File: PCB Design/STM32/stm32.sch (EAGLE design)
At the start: 54 parts, among them Q1 8MHz, T1 SFH303, T2 SFH303, T3 SFH303, T4 SFH303, U1 STM32F103RET6, U2 MCP1700T-3302E/TT, U3 MCP1700T-3302E/TT, U4 MPU-6000QFN-24, U5 TB6612FNG

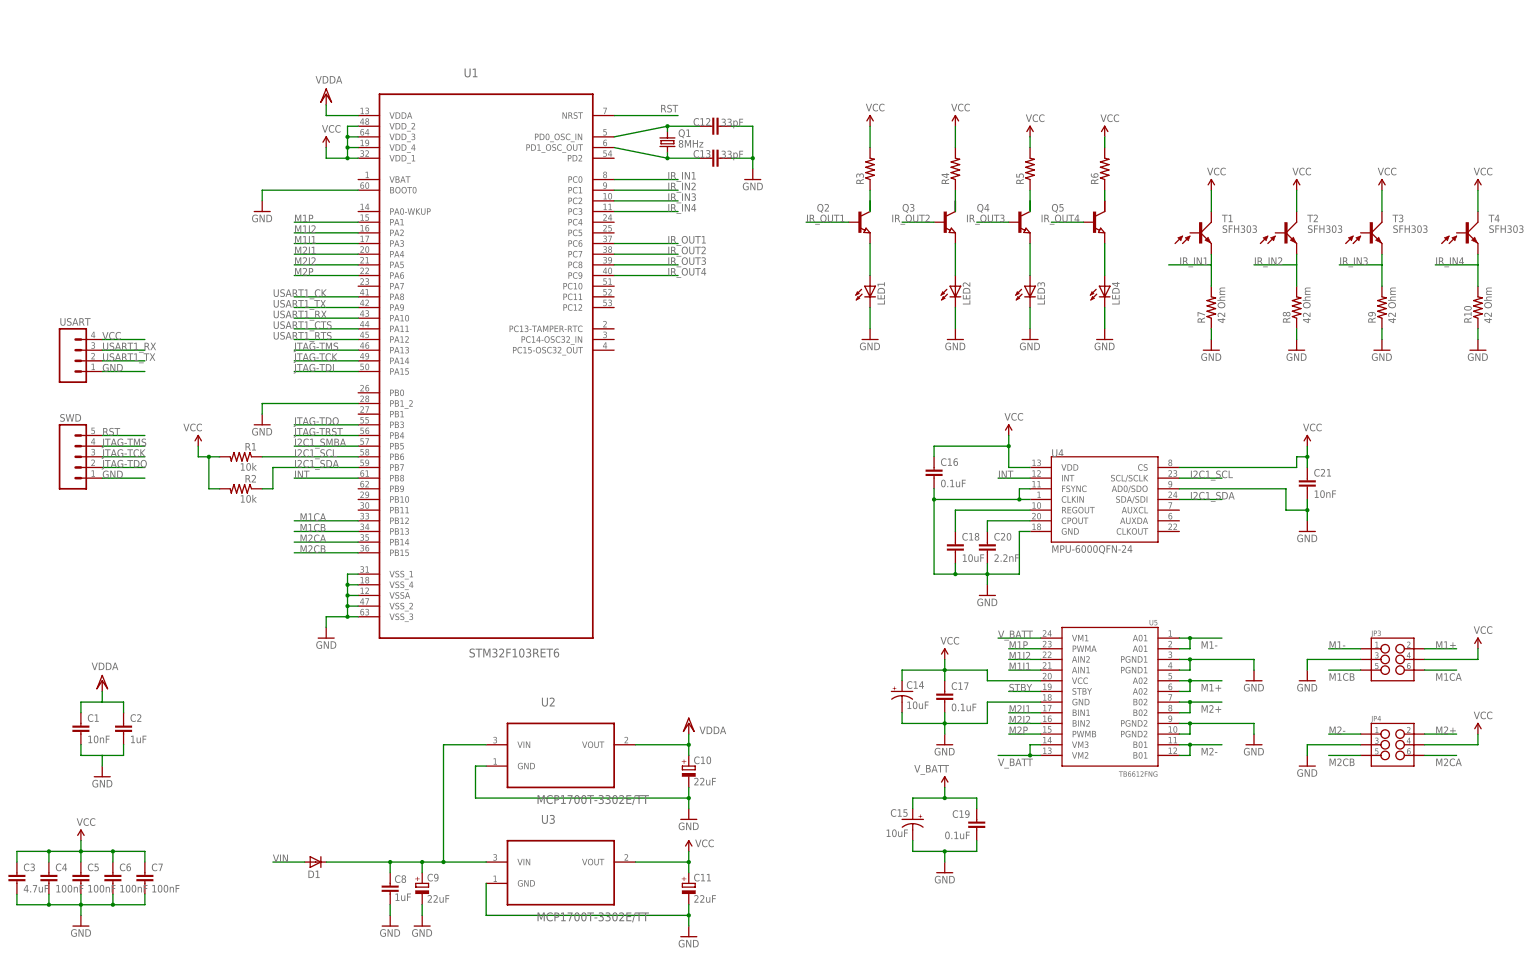
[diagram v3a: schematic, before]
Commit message: add 5v regulator
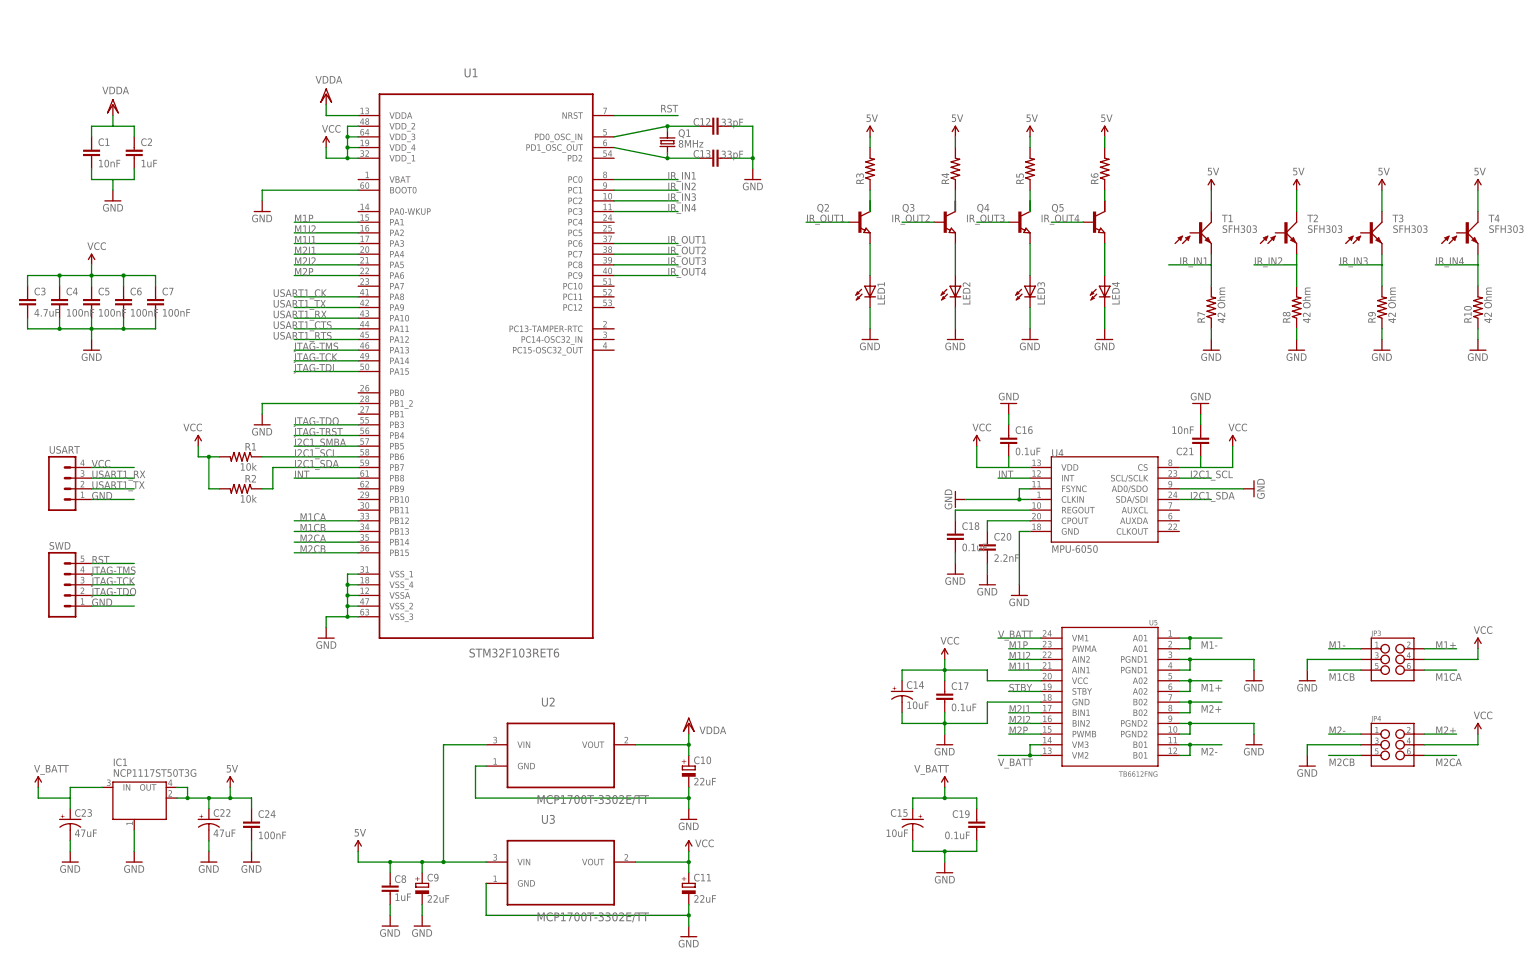
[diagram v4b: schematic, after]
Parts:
- removed D1: (no value), diode:DIODE-SOD323-W
- added C22, C23: 47uF, SparkFun-Capacitors:CAP_POLD
- added C24: 100nF, SparkFun-Capacitors:CAP0603-CAP
- added IC1: NCP1117ST50T3G, linear:MC33269ST-3.3T3
- C18: value 10uF -> 0.1uF
- U4: value MPU-6000QFN-24 -> MPU-6050
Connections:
- removed net N$1: C8.2, C9.+, D1.C, U2.VIN, U3.VIN
- removed net VIN: D1.A
- new net 5V: C22.+, C24.1, C8.2, C9.+, IC1.OUT, IC1.OUT@1, R3.2, R4.2, R5.2, R6.2, T1.C, T2.C, T3.C, T4.C, U2.VIN, U3.VIN
- net GND: now also C16.1, C22.-, C23.-, C24.2, IC1.GND/ADJ; no longer C16.2
- net VCC: now also C16.2; no longer C16.1, R3.2, R4.2, R5.2, R6.2, T1.C, T2.C, T3.C, T4.C
- net V_BATT: now also C23.+, IC1.IN
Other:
- moved on the sheet: C1, C16, C18, C2, C21, C3, C4, C5, C6, C7, SWD, USART

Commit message: refine connection
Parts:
- removed C14: 10uF, SparkFun-Capacitors:CAP_POL1206
- removed C24: 100nF, SparkFun-Capacitors:CAP0603-CAP
- removed C8: 1uF, SparkFun:CAP0603
- C12, C13: device SparkFun:CAP0603 -> SparkFun-Capacitors:CAP0603-CAP
- C15: device SparkFun-Capacitors:CAP_POL1206 -> SparkFun-Capacitors:CAP_POL1206-KIT
- C2: device SparkFun-Capacitors:CAP0603-CAP -> SparkFun-Capacitors:CAP0805
- C22, C23: value 47uF -> 10uF; device SparkFun-Capacitors:CAP_POLD -> rcl:CPOL-EUUD-4X5,8
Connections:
- net 5V: no longer C24.1, C8.2
- net GND: no longer C14.-, C24.2, C8.1
- net STBY: now also U1.PA7
- net VCC: no longer C14.+

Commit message: refine connection
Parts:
- removed C22, C23: 10uF, rcl:CPOL-EUUD-4X5,8
- added C14: 10uF, 33m<ESR<2.2, SparkFun-Capacitors:CAP0805
- added C8: 10uF, SparkFun-Capacitors:CAP0805
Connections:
- net 5V: now also C14.1; no longer C22.+
- net GND: now also C14.2, C8.2; no longer C22.-, C23.-
- net V_BATT: now also C8.1; no longer C23.+
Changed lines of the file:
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@@
 <class number="0" name="default" width="0.254" drill="0">
 </class>
-<class number="1" name="MOTOR" width="0.3048" drill="0">
+<class number="1" name="MOTOR" width="1.016" drill="0">
 </class>
 </classes>
@@
 <part name="GND28" library="SparkFun-Aesthetics" deviceset="GND" device=""/>
 <part name="GND30" library="SparkFun-Aesthetics" deviceset="GND" device=""/>
-<part name="C22" library="rcl" deviceset="CPOL-EU" device="UD-4X5,8" value="10uF"/>
-<part name="C23" library="rcl" deviceset="CPOL-EU" device="UD-4X5,8" value="10uF"/>
 <part name="SUPPLY17" library="SparkFun-Aesthetics" deviceset="5V" device=""/>
 <part name="GND31" library="SparkFun-Aesthetics" deviceset="GND" device=""/>
@@
 <part name="GND35" library="SparkFun-Aesthetics" deviceset="GND" device=""/>
 <part name="SUPPLY18" library="SparkFun-Aesthetics" deviceset="V_BATT" device=""/>
+<part name="C8" library="SparkFun-Capacitors" deviceset="CAP" device="0805" value="10uF"/>
+<part name="C14" library="SparkFun-Capacitors" deviceset="CAP" device="0805" value="10uF, 33m&lt;ESR&lt;2.2"/>
 </parts>
 <sheets>
@@
 <instance part="GND28" gate="1" x="127" y="83.82"/>
 <instance part="GND30" gate="1" x="93.98" y="83.82"/>
-<instance part="C22" gate="G$1" x="127" y="93.98"/>
-<instance part="C23" gate="G$1" x="93.98" y="93.98"/>
 <instance part="SUPPLY17" gate="G$1" x="132.08" y="101.6"/>
 <instance part="GND31" gate="1" x="317.5" y="193.04" rot="R180"/>
@@
 <instance part="GND35" gate="1" x="304.8" y="152.4"/>
 <instance part="SUPPLY18" gate="G$1" x="86.36" y="101.6"/>
+<instance part="C8" gate="G$1" x="93.98" y="91.44"/>
+<instance part="C14" gate="G$1" x="127" y="91.44"/>
 </instances>
 <busses>
@@
 </segment>
 <segment>
-<pinref part="C22" gate="G$1" pin="-"/>
 <pinref part="GND28" gate="1" pin="GND"/>
 <wire x1="127" y1="88.9" x2="127" y2="86.36" width="0.1524" layer="91"/>
-</segment>
-<segment>
-<pinref part="C23" gate="G$1" pin="-"/>
+<pinref part="C14" gate="G$1" pin="2"/>
+</segment>
+<segment>
 <pinref part="GND30" gate="1" pin="GND"/>
 <wire x1="93.98" y1="88.9" x2="93.98" y2="86.36" width="0.1524" layer="91"/>
+<pinref part="C8" gate="G$1" pin="2"/>
 </segment>
 <segment>
@@
 <segment>
 <pinref part="IC1" gate="G$1" pin="IN"/>
-<pinref part="C23" gate="G$1" pin="+"/>
 <wire x1="101.6" y1="101.6" x2="93.98" y2="101.6" width="0.1524" layer="91"/>
 <wire x1="93.98" y1="101.6" x2="93.98" y2="99.06" width="0.1524" layer="91"/>
@@
 <wire x1="86.36" y1="99.06" x2="86.36" y2="101.6" width="0.1524" layer="91"/>
 <junction x="93.98" y="99.06"/>
+<pinref part="C8" gate="G$1" pin="1"/>
 </segment>
 </net>
@@
 <wire x1="127" y1="99.06" x2="132.08" y2="99.06" width="0.1524" layer="91"/>
 <wire x1="121.92" y1="101.6" x2="121.92" y2="99.06" width="0.1524" layer="91"/>
-<pinref part="C22" gate="G$1" pin="+"/>
 <wire x1="127" y1="99.06" x2="127" y2="96.52" width="0.1524" layer="91"/>
 <junction x="121.92" y="99.06"/>
@@
 <pinref part="SUPPLY17" gate="G$1" pin="5V"/>
 <wire x1="132.08" y1="101.6" x2="132.08" y2="99.06" width="0.1524" layer="91"/>
-</segment>
-</net>
+<pinref part="C14" gate="G$1" pin="1"/>
+</segment>
+</net>

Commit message: meeting update
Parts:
- added R11, R12, R13, R14: (no value), resistor:R-US_R0603
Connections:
- new net N$22: Q5.B, R14.1
- new net N$23: Q4.B, R13.1
- new net N$24: Q3.B, R12.1
- new net N$25: Q2.B, R11.1
- net 5V: now also LED1.A, LED2.A, LED3.A, LED4.A; no longer R3.2, R4.2, R5.2, R6.2
- net GND: now also R3.1, R4.1, R5.1, R6.1; no longer LED1.C, LED2.C, LED3.C, LED4.C
- net IR_OUT1: now also R11.2; no longer Q2.B
- net IR_OUT2: now also R12.2; no longer Q3.B
- net IR_OUT3: now also R13.2; no longer Q4.B
- net IR_OUT4: now also R14.2; no longer Q5.B
- net N$14: now also R3.2; no longer LED1.A
- net N$15: now also R4.2; no longer LED2.A
- net N$16: now also R5.2; no longer LED3.A
- net N$17: now also R6.2; no longer LED4.A
- net N$3: now also LED1.C, Q2.C; no longer Q2.C/, R3.1
- net N$4: now also LED2.C, Q3.C; no longer Q3.C/, R4.1
- net N$5: now also LED3.C, Q4.C; no longer Q4.C/, R5.1
- net N$7: now also LED4.C; no longer R6.1
- net STBY: no longer U5.STBY
- net VCC: now also U5.STBY
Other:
- moved on the sheet: LED1, LED2, LED3, LED4, Q2, Q3, Q5, R3, R4, R5, R6
